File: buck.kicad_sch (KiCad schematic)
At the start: 32 parts, among them J6 Conn_01x02_Socket, Q1 RS1G120MNTB, Q2 RS1G120MNTB, U5 BQ24640

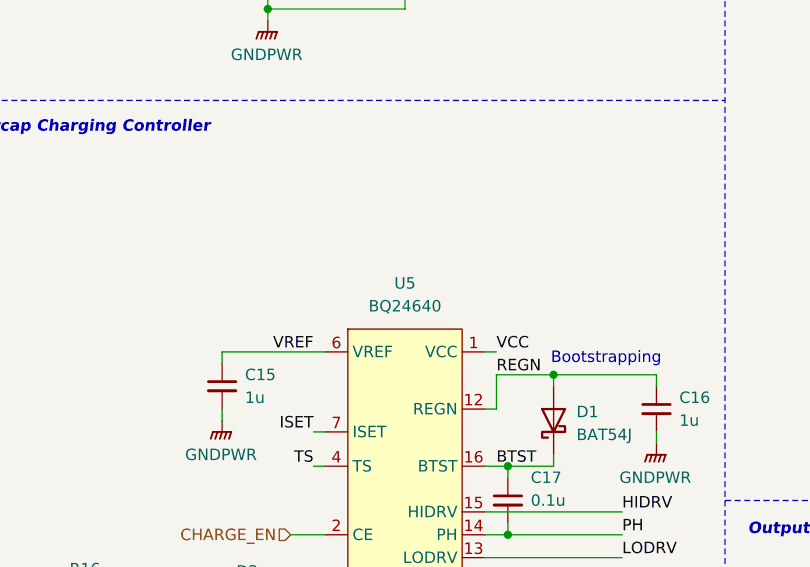
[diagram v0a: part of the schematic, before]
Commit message: Correct symbol library path, renumber components
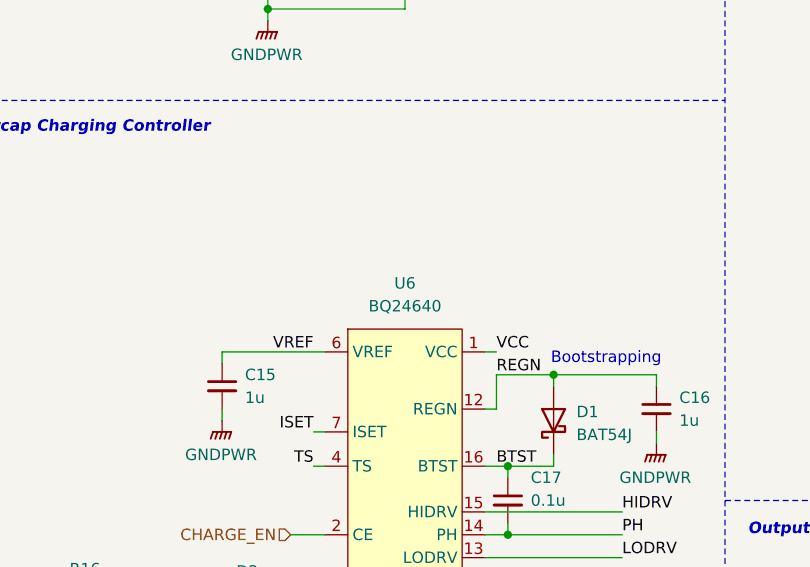
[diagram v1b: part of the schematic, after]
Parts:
- renumbered U5 to U6
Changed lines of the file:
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@@
 		(dnp no)
 		(fields_autoplaced yes)
-		(property "Reference" "U5"
+		(property "Reference" "U6"
 			(at 67.31 80.01 0)
 			(effects
@@
 			(project ""
 				(path "/6197145b-e7d4-44cc-9d90-537b6501bf60/388608c4-ca49-4b14-9684-8f150e280879"
-					(reference "U5")
+					(reference "U6")
 					(unit 1)
 				)

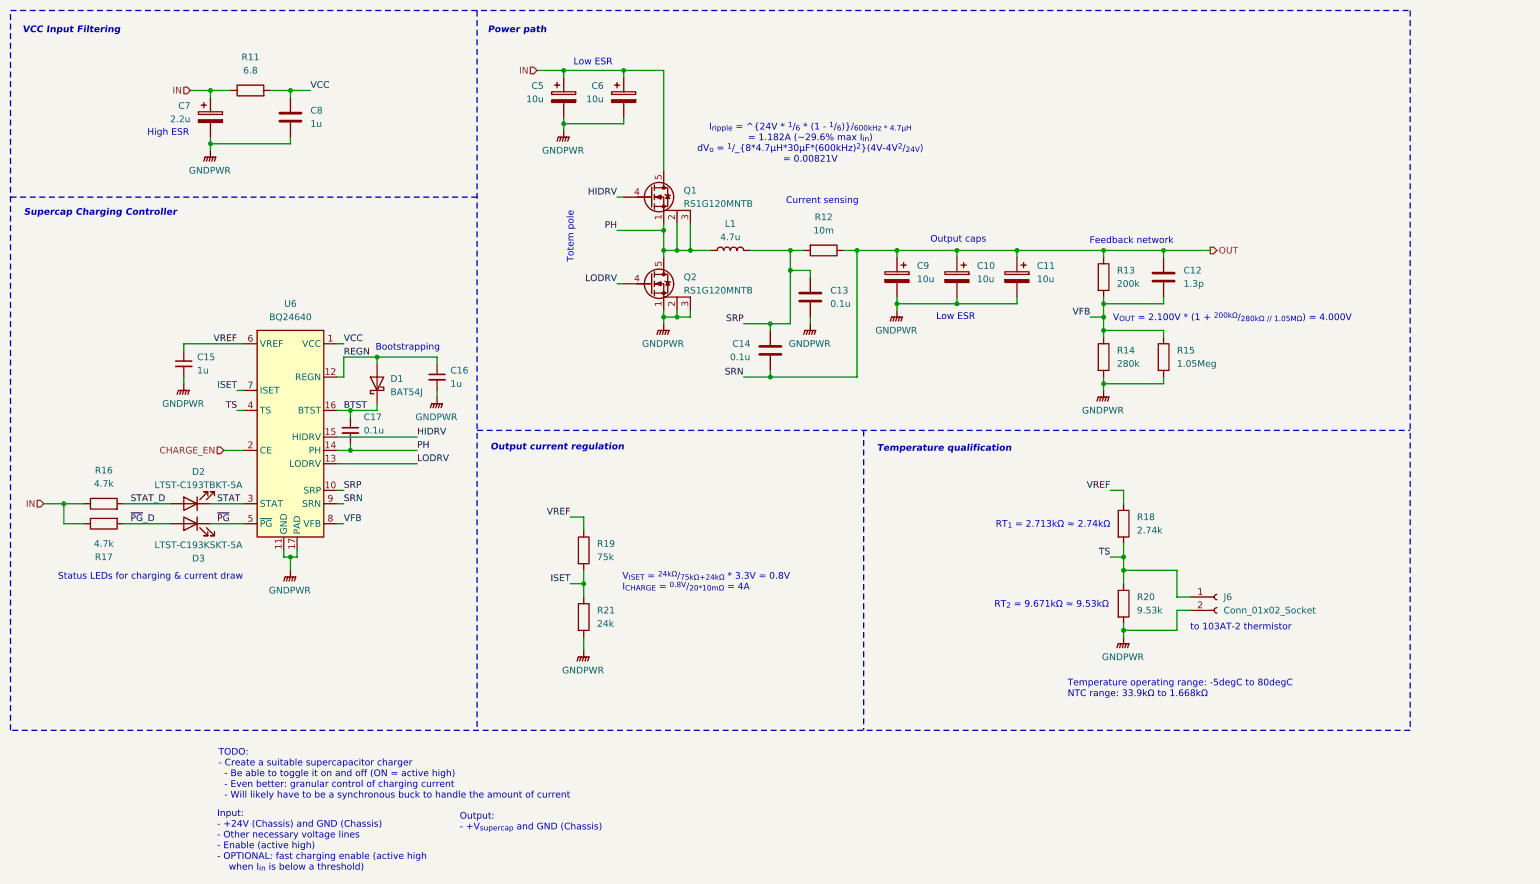
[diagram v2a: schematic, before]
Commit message: Layout iteration 1 for the input buck
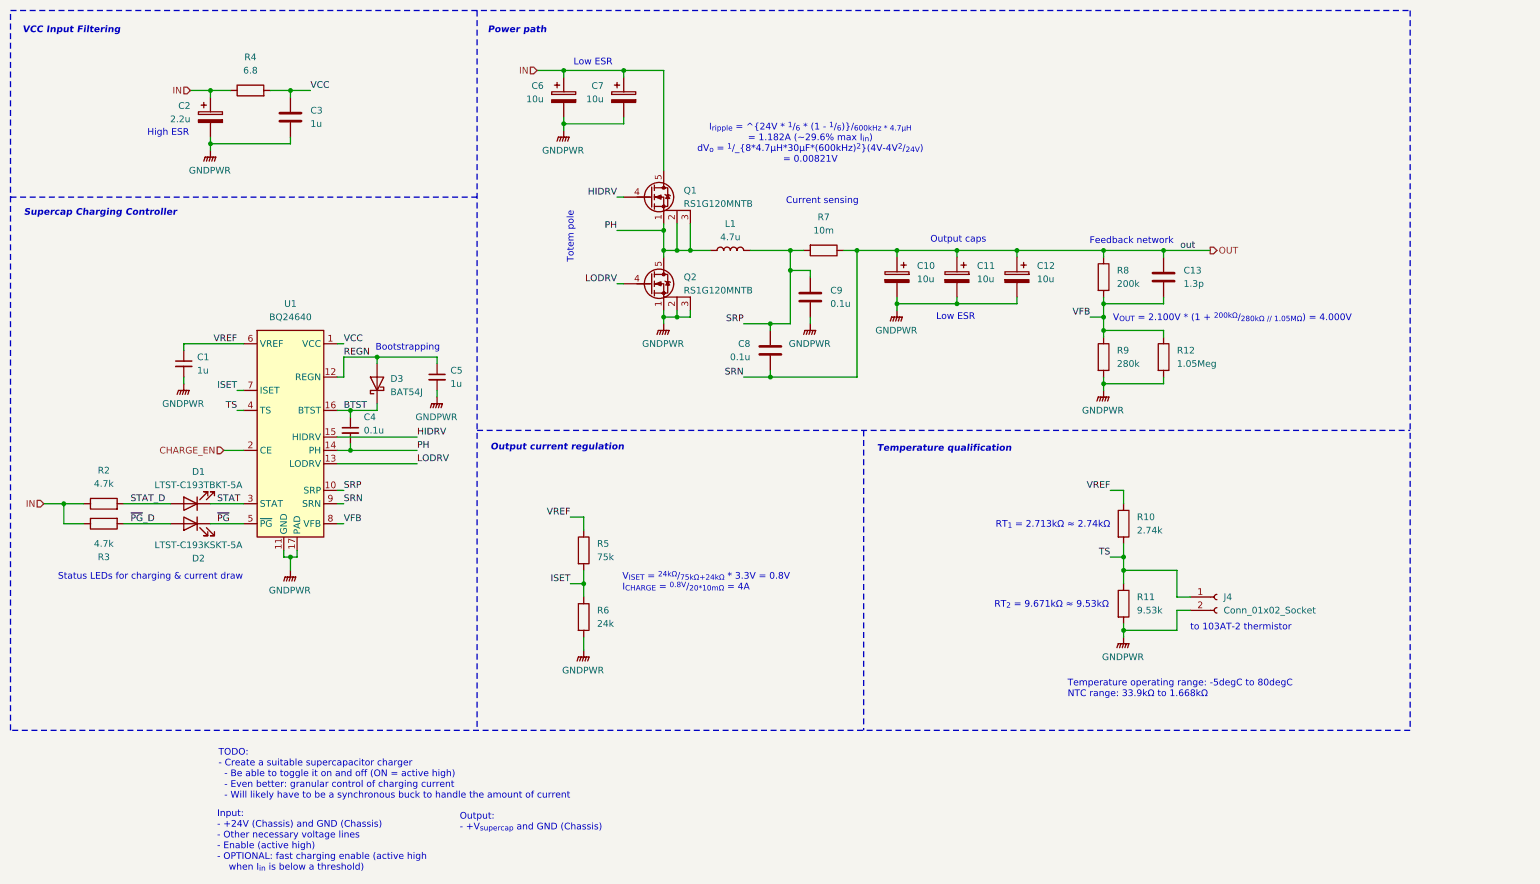
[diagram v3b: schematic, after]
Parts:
- renumbered C15 to C1, C9 to C10, C10 to C11, C11 to C12, C12 to C13, C7 to C2, C8 to C3, C17 to C4, C16 to C5, C5 to C6, C6 to C7, C14 to C8, C13 to C9, D2 to D1, D3 to D2, D1 to D3, J6 to J4, R18 to R10, R20 to R11, R15 to R12, R16 to R2, R17 to R3, R11 to R4, R19 to R5, R21 to R6, R12 to R7, R13 to R8, R14 to R9, U6 to U1

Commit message: Minor changes
Still need to replace the inductor footprint with the correct one
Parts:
- L1: footprint (none) -> Inductor_SMD:L_0603_1608Metric_Pad1.05x0.95mm_HandSolder
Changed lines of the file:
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@@
-		)
-	)
-	(label "out"
-		(at 236.855 69.85 0)
-		(effects
-			(font
-				(size 1.27 1.27)
-			)
-			(justify left bottom)
 		)
 	)
@@
 			)
 		)
-		(property "Footprint" ""
+		(property "Footprint" "Inductor_SMD:L_0603_1608Metric_Pad1.05x0.95mm_HandSolder"
 			(at 151.13 69.85 0)
 			(effects
@@
 			)
 		)
+		(property "Mouser #" ""
+			(at 151.13 69.85 0)
+			(effects
+				(font
+					(size 1.27 1.27)
+				)
+				(hide yes)
+			)
+		)
+		(property "Mouser Link" ""
+			(at 151.13 69.85 0)
+			(effects
+				(font
+					(size 1.27 1.27)
+				)
+				(hide yes)
+			)
+		)
+		(property "JLCPCB #" ""
+			(at 151.13 69.85 0)
+			(effects
+				(font
+					(size 1.27 1.27)
+				)
+				(hide yes)
+			)
+		)

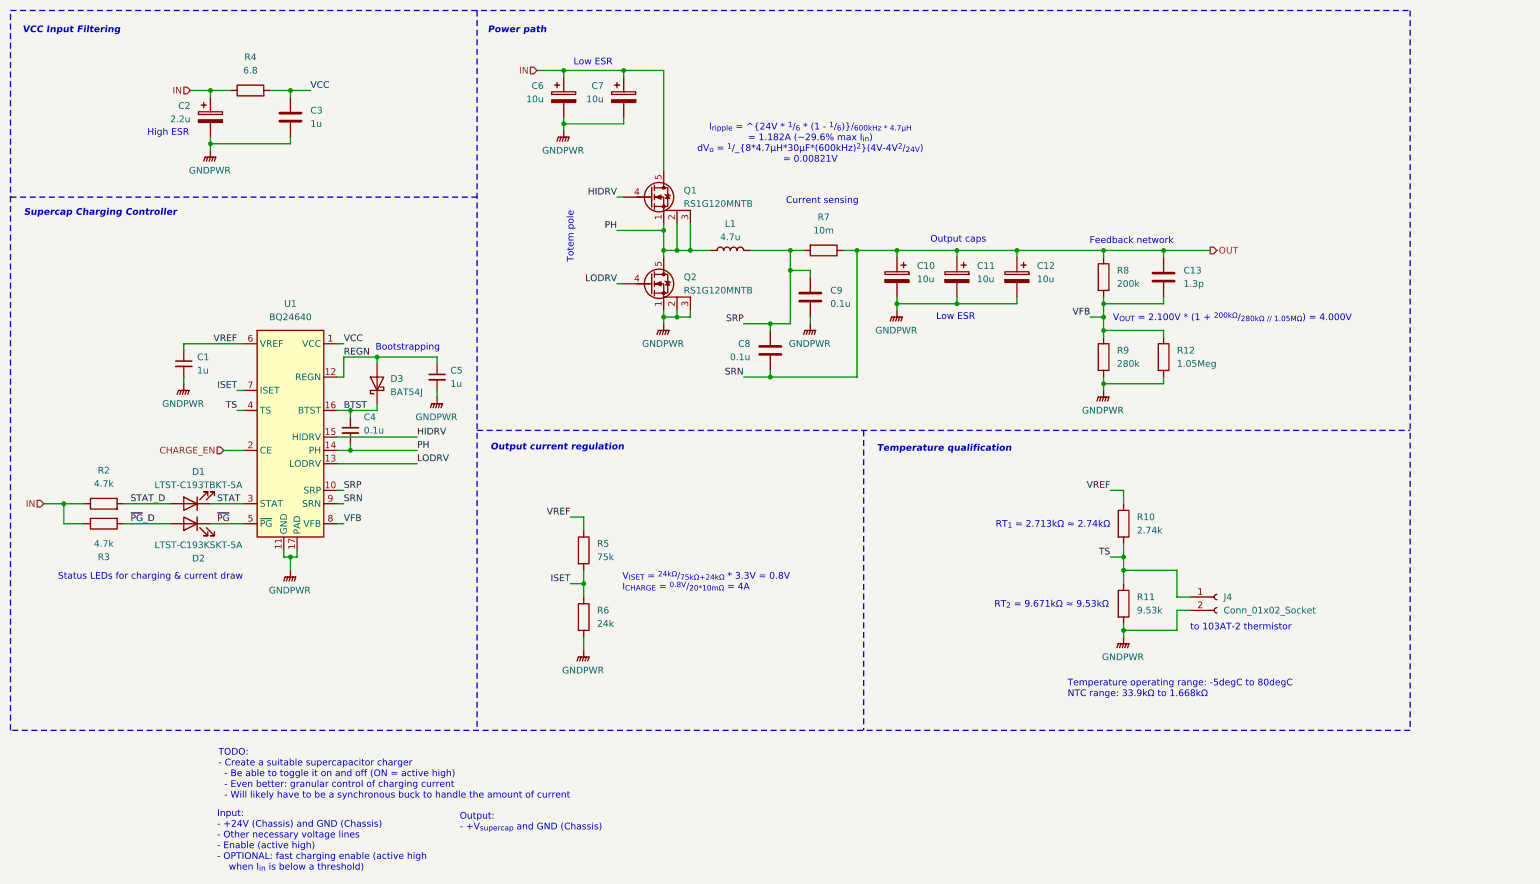
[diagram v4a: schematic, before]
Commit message: Completed stage 2 schematic
+ added SPICE models for all the custom components
+ renumbered components
+ updated library with stage 2 symbols
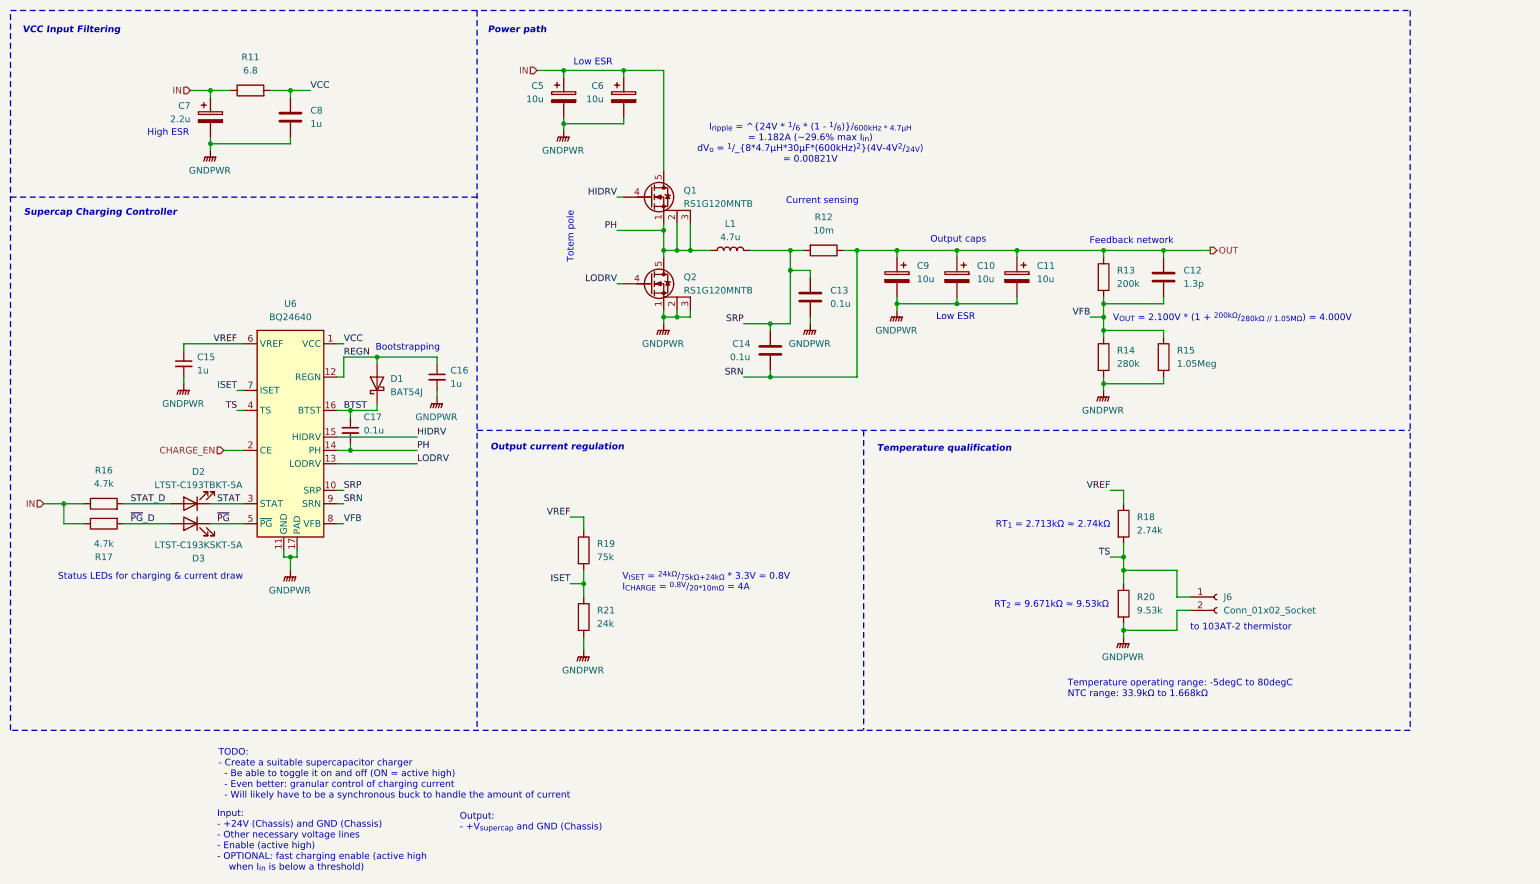
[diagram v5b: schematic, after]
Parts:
- renumbered C11 to C10, C12 to C11, C13 to C12, C9 to C13, C8 to C14, C1 to C15, C5 to C16, C4 to C17, C6 to C5, C7 to C6, C2 to C7, C3 to C8, C10 to C9, D3 to D1, D1 to D2, D2 to D3, J4 to J6, R4 to R11, R7 to R12, R8 to R13, R9 to R14, R12 to R15, R2 to R16, R3 to R17, R10 to R18, R5 to R19, R11 to R20, R6 to R21, U1 to U6
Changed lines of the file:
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@@
 		(on_board yes)
 		(dnp no)
-		(property "Reference" "C11"
+		(property "Reference" "C10"
 			(at 198.12 72.7709 0)
 			(effects
@@
 		(dnp no)
 		(fields_autoplaced yes)
-		(property "Reference" "R8"
+		(property "Reference" "R13"
 			(at 224.79 73.6599 0)
 			(effects
@@
 		(dnp no)
 		(fields_autoplaced yes)
-		(property "Reference" "#PWR0102"
+		(property "Reference" "#PWR031"
 			(at 182.88 86.36 0)
 			(effects
@@
 		(dnp no)
 		(fields_autoplaced yes)
-		(property "Reference" "R11"
+		(property "Reference" "R20"
 			(at 228.6 135.8899 0)
 			(effects
@@
 		(dnp no)
 		(fields_autoplaced yes)
-		(property "Reference" "#PWR0109"
+		(property "Reference" "#PWR036"
 			(at 95.25 102.87 0)
 			(effects
@@
 		(on_board yes)
 		(dnp no)
-		(property "Reference" "D2"
+		(property "Reference" "D3"
 			(at 49.784 128.524 0)
 			(effects
@@
 		(dnp no)
 		(fields_autoplaced yes)
-		(property "Reference" "#PWR0107"
+		(property "Reference" "#PWR039"
 			(at 123.19 151.13 0)
 			(effects
@@
 		(dnp no)
 		(fields_autoplaced yes)
-		(property "Reference" "U1"
+		(property "Reference" "U6"
 			(at 67.31 80.01 0)
 			(effects
@@
 		(on_board yes)
 		(dnp no)
-		(property "Reference" "C6"
+		(property "Reference" "C5"
 			(at 115.57 38.4809 0)
 			(effects
@@
 		(dnp no)
 		(fields_autoplaced yes)
-		(property "Reference" "#PWR0105"
+		(property "Reference" "#PWR038"
 			(at 226.06 148.59 0)
 			(effects
@@
 		(dnp no)
 		(fields_autoplaced yes)
-		(property "Reference" "R4"
+		(property "Reference" "R11"
 			(at 59.69 33.02 90)
 			(effects
@@
 		(on_board yes)
 		(dnp no)
-		(property "Reference" "R3"
+		(property "Reference" "R17"
 			(at 31.75 128.27 90)
 			(effects
@@
 		(dnp no)
 		(fields_autoplaced yes)
-		(property "Reference" "C5"
+		(property "Reference" "C16"
 			(at 97.79 92.7162 0)
 			(effects
@@
 		(dnp no)
 		(fields_autoplaced yes)
-		(property "Reference" "R12"
+		(property "Reference" "R15"
 			(at 236.22 88.8999 0)
 			(effects
@@
 		(dnp no)
 		(fields_autoplaced yes)
-		(property "Reference" "#PWR0106"
+		(property "Reference" "#PWR037"
 			(at 67.31 135.89 0)
 			(effects
@@
 		(on_board yes)
 		(dnp no)
-		(property "Reference" "C2"
+		(property "Reference" "C7"
 			(at 48.26 42.2909 0)
 			(effects
@@
 		(on_board yes)
 		(dnp no)
-		(property "Reference" "D1"
+		(property "Reference" "D2"
 			(at 49.784 112.014 0)
 			(effects
@@
 		(dnp no)
 		(fields_autoplaced yes)
-		(property "Reference" "J4"
+		(property "Reference" "J6"
 			(at 245.11 135.8899 0)
 			(effects
@@
 		(dnp no)
 		(fields_autoplaced yes)
-		(property "Reference" "C1"
+		(property "Reference" "C15"
 			(at 49.53 90.1762 0)
 			(effects
@@
 		(dnp no)
 		(fields_autoplaced yes)
-		(property "Reference" "D3"
+		(property "Reference" "D1"
 			(at 86.36 94.2974 90)
 			(effects
@@
 		(dnp no)
 		(fields_autoplaced yes)
-		(property "Reference" "R6"
+		(property "Reference" "R21"
 			(at 125.73 138.4299 0)
 			(effects
@@
 		(on_board yes)
 		(dnp no)
-		(property "Reference" "C10"
+		(property "Reference" "C9"
 			(at 186.69 72.7709 0)
 			(effects
@@
 		(dnp no)
 		(fields_autoplaced yes)
-		(property "Reference" "R10"
+		(property "Reference" "R18"
 			(at 228.6 120.6499 0)
 			(effects
@@
 		(dnp no)
 		(fields_autoplaced yes)
-		(property "Reference" "R5"
+		(property "Reference" "R19"
 			(at 125.73 125.7299 0)
 			(effects
@@
 		(dnp no)
 		(fields_autoplaced yes)
-		(property "Reference" "#PWR0111"
+		(property "Reference" "#PWR034"
 			(at 46.99 100.33 0)
 			(effects
@@
 		(dnp no)
 		(fields_autoplaced yes)
-		(property "Reference" "#PWR0101"
+		(property "Reference" "#PWR035"
 			(at 222.25 101.6 0)
 			(effects
@@
 		(on_board yes)
 		(dnp no)
-		(property "Reference" "C8"
+		(property "Reference" "C14"
 			(at 154.94 87.6299 0)
 			(effects
@@
 		(dnp no)
 		(fields_autoplaced yes)
-		(property "Reference" "C9"
+		(property "Reference" "C13"
 			(at 170.18 77.4699 0)
 			(effects
@@
 		(dnp no)
 		(fields_autoplaced yes)
-		(property "Reference" "R9"
+		(property "Reference" "R14"
 			(at 224.79 88.8999 0)
 			(effects
@@
 		(dnp no)
 		(fields_autoplaced yes)
-		(property "Reference" "R7"
+		(property "Reference" "R12"
 			(at 168.91 63.5 90)
 			(effects
@@
 		(dnp no)
 		(fields_autoplaced yes)
-		(property "Reference" "R2"
+		(property "Reference" "R16"
 			(at 31.75 111.76 90)
 			(effects
@@
 		(dnp no)
 		(fields_autoplaced yes)
-		(property "Reference" "#PWR0108"
+		(property "Reference" "#PWR029"
 			(at 119.38 52.07 0)
 			(effects
@@
 		(dnp no)
 		(fields_autoplaced yes)
-		(property "Reference" "C13"
+		(property "Reference" "C12"
 			(at 237.49 73.6599 0)
 			(effects
@@
 		(dnp no)
 		(fields_autoplaced yes)
-		(property "Reference" "#PWR0110"
+		(property "Reference" "#PWR030"
 			(at 52.07 55.88 0)
 			(effects
@@
 		(dnp no)
 		(fields_autoplaced yes)
-		(property "Reference" "#PWR0103"
+		(property "Reference" "#PWR033"
 			(at 166.37 88.9 0)
 			(effects
@@
 		(dnp no)
 		(fields_autoplaced yes)
-		(property "Reference" "#PWR0104"
+		(property "Reference" "#PWR032"
 			(at 138.43 88.9 0)
 			(effects
@@
 		(on_board yes)
 		(dnp no)
-		(property "Reference" "C7"
+		(property "Reference" "C6"
 			(at 127 38.4809 0)
 			(effects
@@
 		(on_board yes)
 		(dnp no)
-		(property "Reference" "C4"
+		(property "Reference" "C17"
 			(at 81.28 101.6 0)
 			(effects
@@
 		(dnp no)
 		(fields_autoplaced yes)
-		(property "Reference" "C3"
+		(property "Reference" "C8"
 			(at 71.12 43.1799 0)
 			(effects
@@
 		(on_board yes)
 		(dnp no)
-		(property "Reference" "C12"
+		(property "Reference" "C11"
 			(at 209.55 72.7709 0)
 			(effects
